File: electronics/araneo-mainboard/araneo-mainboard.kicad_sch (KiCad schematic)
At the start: 69 parts, among them J2 OLED, J3 GPIO, SW1 SW, SW2 SW, U1 IMU, U2 L78M05CDT, U3 BD9C601EFJ, U4 POWER, U5 PAM8403D

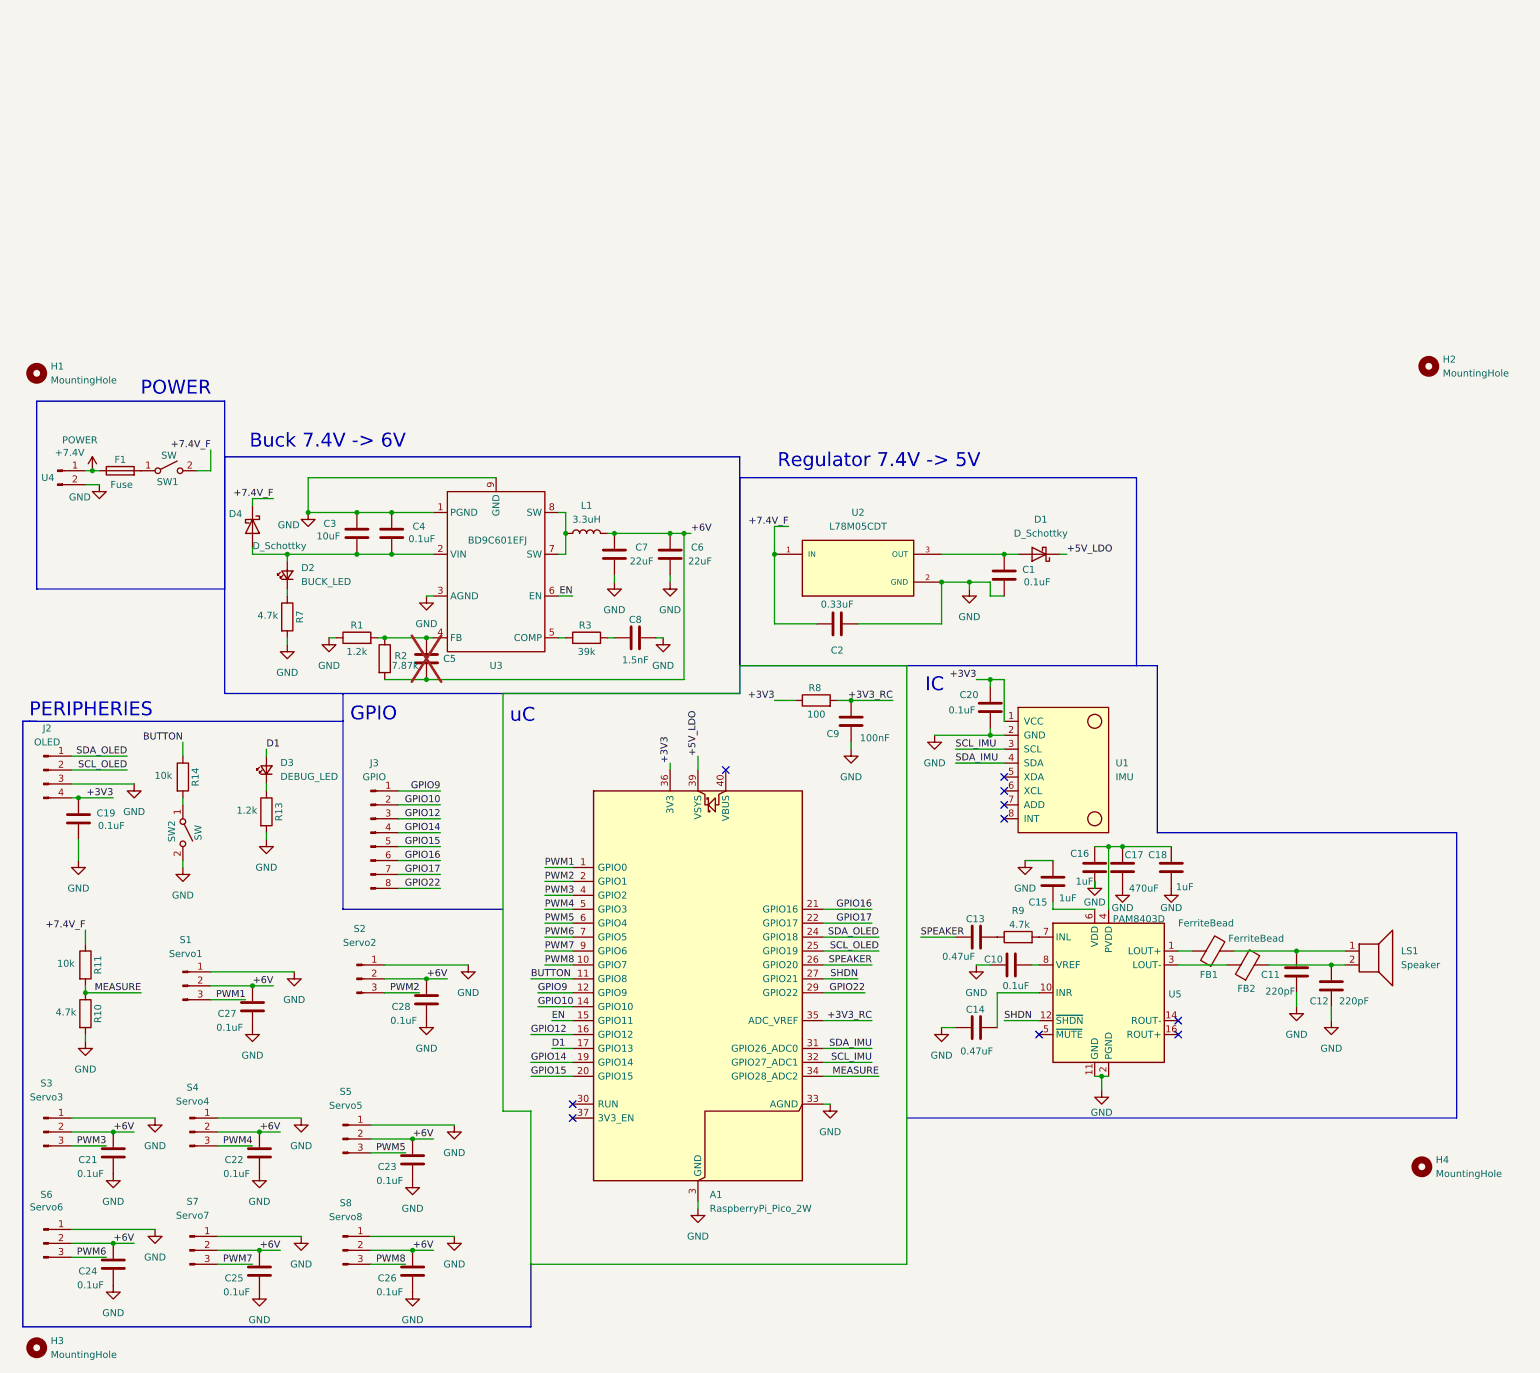
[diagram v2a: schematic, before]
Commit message: electronics: new buck, regulator and improve schematic
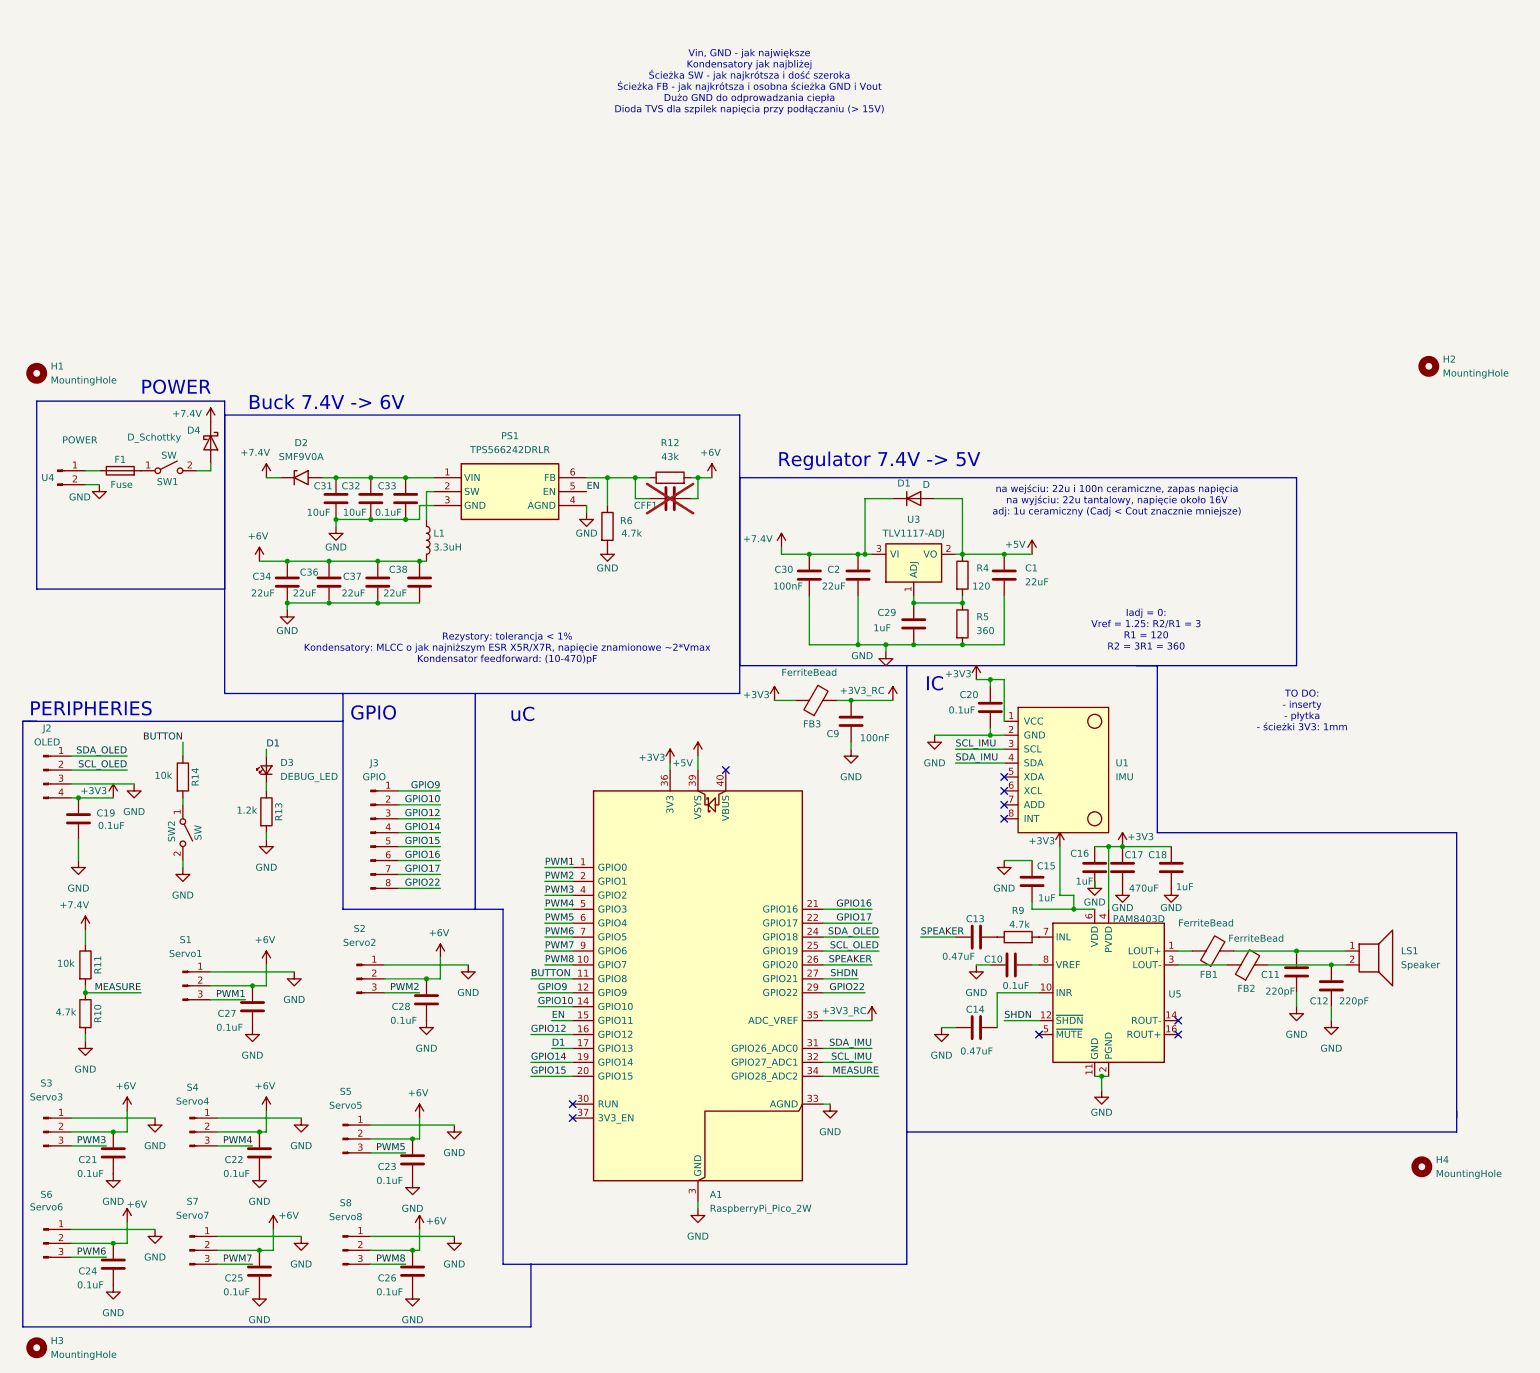
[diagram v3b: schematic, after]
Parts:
- removed C3: 10uF, Capacitor_SMD:C_1206_3216Metric_Pad1.33x1.80mm_HandSolder, symbol Device:C
- removed C4: 0.1uF, Capacitor_SMD:C_0603_1608Metric_Pad1.08x0.95mm_HandSolder, symbol Device:C
- removed C5: OPEN, Capacitor_SMD:C_0603_1608Metric_Pad1.08x0.95mm_HandSolder, symbol Device:C
- removed C6, C7: 22uF, Capacitor_SMD:C_1210_3225Metric_Pad1.33x2.70mm_HandSolder, symbol Device:C
- removed C8: 1.5nF, Capacitor_SMD:C_0603_1608Metric_Pad1.08x0.95mm_HandSolder, symbol Device:C
- removed D1: D_Schottky, Diode_THT:D_DO-41_SOD81_P10.16mm_Horizontal, symbol Device:D_Schottky
- removed D2: BUCK_LED, PCM_SparkFun-LED:LED_0603_1608Metric, symbol PCM_SparkFun-LED:LED
- removed R1: 1.2k, Resistor_SMD:R_0603_1608Metric_Pad0.98x0.95mm_HandSolder, symbol Device:R
- removed R2: 7.87k, Resistor_SMD:R_0603_1608Metric_Pad0.98x0.95mm_HandSolder, symbol Device:R
- removed R3: 39k, Resistor_SMD:R_0603_1608Metric_Pad0.98x0.95mm_HandSolder, symbol Device:R
- removed R7: 4.7k, Resistor_SMD:R_0603_1608Metric_Pad0.98x0.95mm_HandSolder, symbol Device:R
- removed R8: 100, Resistor_SMD:R_0603_1608Metric_Pad0.98x0.95mm_HandSolder, symbol Device:R
- removed U2: L78M05CDT, custom_footprints:VREG_L78M05CDT, symbol Symbols:L78M05CDT
- removed U3: BD9C601EFJ, custom_footprints:SOIC127P600X100-9N, symbol Custom_Regulators:BD9C601EFJ
- added C29: 1uF, Capacitor_SMD:C_0603_1608Metric_Pad1.08x0.95mm_HandSolder, symbol Device:C
- added C30, CFF1: 100nF, Capacitor_SMD:C_0603_1608Metric_Pad1.08x0.95mm_HandSolder, symbol Device:C
- added C31, C32: 10uF, Capacitor_SMD:C_1206_3216Metric_Pad1.33x1.80mm_HandSolder, symbol Device:C
- added C33: 0.1uF, Capacitor_SMD:C_0201_0603Metric_Pad0.64x0.40mm_HandSolder, symbol Device:C
- added C34, C36, C37, C38: 22uF, Capacitor_SMD:C_1210_3225Metric_Pad1.33x2.70mm_HandSolder, symbol Device:C
- added D1: D, Diode_THT:D_DO-41_SOD81_P10.16mm_Horizontal, symbol Device:D
- added D2: SMF9V0A, Diode_SMD:D_SMF, symbol Diode:SMF9V0A
- added FB3: FerriteBead, Resistor_SMD:R_0603_1608Metric_Pad0.98x0.95mm_HandSolder, symbol Device:FerriteBead
- added PS1: TPS566242DRLR, custom_footprints:SOT50P160X60-6N, symbol Symbols:TPS566242DRLR
- added R12: 43k, Resistor_SMD:R_0603_1608Metric_Pad0.98x0.95mm_HandSolder, symbol Device:R
- added R4: 120, Resistor_SMD:R_0603_1608Metric_Pad0.98x0.95mm_HandSolder, symbol Device:R
- added R5: 360, Resistor_SMD:R_0603_1608Metric_Pad0.98x0.95mm_HandSolder, symbol Device:R
- added R6: 4.7k, Resistor_SMD:R_0603_1608Metric_Pad0.98x0.95mm_HandSolder, symbol Device:R
- added U3: TLV1117-ADJ, Package_TO_SOT_SMD:SOT-223-3_TabPin2, symbol Regulator_Linear:TLV1117-ADJ
- C1: value 0.1uF -> 22uF; footprint Capacitor_SMD:C_0603_1608Metric_Pad1.08x0.95mm_HandSolder -> Capacitor_Tantalum_SMD:CP_EIA-3528-15_AVX-H_HandSolder
- C2: value 0.33uF -> 22uF; footprint Capacitor_SMD:C_0805_2012Metric_Pad1.18x1.45mm_HandSolder -> Capacitor_SMD:C_1210_3225Metric_Pad1.33x2.70mm_HandSolder
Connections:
- net +5V_LDO is gone; now on net +5V: A1.39 (VSYS)
- net +3V3: now also C15.1, C16.2, C17.2, C18.2, U5.13 (PVDD), U5.4 (PVDD), U5.6 (VDD), FB3.1
- net +3V3_RC: now also FB3.2
- net +6V: now also C34.1, C36.1, C37.1, C38.1, CFF1.2, R12.2
- net +7.4V: now also C2.1, D4.1 (K), R11.1, C30.1, D1.1 (K), D2.1 (A1), U3.3 (VI); no longer F1.1, U4.1 (Pin_1)
- net EN: now also PS1.5 (EN)
- net GND: now also C29.2, C30.2, C31.2, C32.2, C33.2, C34.2, C36.2, C37.2, C38.2, PS1.3 (GND), PS1.4 (AGND), R5.2, R6.2
- net at D4.2 (A): now also SW1.2 (B)
- net at L1.1: now also PS1.2 (SW)
- net +5V: now reaches C1.1
- net +5V: now also D1.2 (A), R4.1, U3.2 (VO)
- removed net +7.4V_F: C2.1, D4.1 (K), R11.1, SW1.2 (B)
- new net: F1.1, U4.1 (Pin_1)
- new net: CFF1.1, PS1.6 (FB), R12.1, R6.1
- new net: C31.1, C32.1, C33.1, D2.2 (A2), PS1.1 (VIN)
- new net: C29.1, R4.2, R5.1, U3.1 (ADJ)
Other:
- note added: "Iadj = 0: Vref = 1.25: R2/R1 = 3 R1 = 120 R2 = 3R1 = 360"
- note added: "Rezystory: tolerancja < 1% Kondensatory: MLCC o jak najniższym ESR X5R/X7R, napięcie znamionowe ~2*Vmax Kondensator feedforward: (10-470)pF"
- note added: "TO DO: - inserty - płytka - ścieżki 3V3: 1mm"
- note added: "Vin, GND - jak największe Kondensatory jak najbliżej Ścieżka SW - jak najkrótsza i dość szeroka Ścieżka FB - jak najkrótsza i osobna ścieżka GND i Vout Dużo GND do odprowadzania ciepła Dioda TVS dla szpilek napięcia przy podłączaniu (> 15V)"
- note added: "na wejściu: 22u i 100n ceramiczne, zapas napięcia na wyjściu: 22u tantalowy, napięcie około 16V adj: 1u ceramiczny (Cadj < Cout znacznie mniejsze)"
- moved on the sheet: C15

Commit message: electronics: pcb v3
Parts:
- removed D4: D_Schottky, Diode_THT:D_DO-41_SOD81_P10.16mm_Horizontal, symbol Device:D_Schottky
- removed F1: Fuse, custom_footprints:3568, symbol Device:Fuse
- removed J3: GPIO, Connector_PinHeader_2.54mm:PinHeader_1x08_P2.54mm_Vertical, symbol Connector:Conn_01x08_Pin
- removed SW1: SW, PCM_SparkFun-Connector:ScrewTerminal_1x02_P5.0mm, symbol Switch:SW_SPST
- added D5: POWER_LED, PCM_SparkFun-LED:LED_0603_1608Metric, symbol PCM_SparkFun-LED:LED
- added D6: D_Schottky, Diode_THT:D_DO-41_SOD81_P10.16mm_Horizontal, symbol Device:D_Schottky
- added F2: Fuse, custom_footprints:3568, symbol Device:Fuse
- added J1: GPIO2, Connector_PinHeader_2.54mm:PinHeader_1x06_P2.54mm_Vertical, symbol Connector:Conn_01x06_Pin
- added J3: GPIO1, Connector_PinHeader_2.54mm:PinHeader_1x02_P2.54mm_Vertical, symbol Connector:Conn_01x02_Pin
- added R15: 1k, Resistor_SMD:R_0603_1608Metric_Pad0.98x0.95mm_HandSolder, symbol Device:R
- added SW3: SW, PCM_SparkFun-Connector:ScrewTerminal_1x02_P5.0mm, symbol Switch:SW_SPST
- C33: footprint Capacitor_SMD:C_0201_0603Metric_Pad0.64x0.40mm_HandSolder -> Capacitor_SMD:C_0603_1608Metric_Pad1.08x0.95mm_HandSolder
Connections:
- net GPIO16 is gone; now on net SDA_OLED: A1.21 (GPIO16)
- net GPIO17 is gone; now on net SCL_OLED: A1.22 (GPIO17)
- net GPIO22 is gone; now on net D1: A1.29 (GPIO22)
- net GPIO9 is gone; now on net PWM8: A1.12 (GPIO9)
- net +7.4V: now also U4.1 (Pin_1), D6.1 (K); no longer C2.1, C30.1, D1.1 (K), D2.1 (A1), R11.1, U3.3 (VI)
- net BUTTON: now also A1.2 (GPIO1); no longer A1.11 (GPIO8)
- net D1: no longer A1.17 (GPIO13)
- net EN: now also A1.1 (GPIO0); no longer A1.15 (GPIO11)
- net GND: now also R15.1
- net GPIO10: now also J1.1 (Pin_1)
- net GPIO12: now also J1.3 (Pin_3)
- net GPIO14: now also J1.5 (Pin_5)
- net GPIO15: now also J1.6 (Pin_6)
- net PWM1: now also A1.4 (GPIO2); no longer A1.1 (GPIO0)
- net PWM2: now also A1.5 (GPIO3); no longer A1.2 (GPIO1)
- net PWM3: now also A1.6 (GPIO4); no longer A1.4 (GPIO2)
- net PWM4: now also A1.7 (GPIO5); no longer A1.5 (GPIO3)
- net PWM5: now also A1.9 (GPIO6); no longer A1.6 (GPIO4)
- net PWM6: now also A1.10 (GPIO7); no longer A1.7 (GPIO5)
- net PWM7: now also A1.11 (GPIO8); no longer A1.9 (GPIO6)
- net PWM8: no longer A1.10 (GPIO7)
- net SCL_OLED: no longer A1.25 (GPIO19)
- net SDA_OLED: no longer A1.24 (GPIO18)
- net SHDN: now also A1.26 (GPIO20); no longer A1.27 (GPIO21)
- net SPEAKER: now also A1.27 (GPIO21); no longer A1.26 (GPIO20)
- net at C31.1, C32.1, C33.1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: now also D5.2 (A)
- new net: F2.2, SW3.2 (B)
- new net: D6.2 (A), SW3.1 (A)
- new net: D5.1 (K), R15.2
- new net +7.4V_F: C2.1, C30.1, D1.1 (K), D2.1 (A1), F2.1, R11.1, U3.3 (VI)
- new net GPIO11: A1.15 (GPIO11), J1.2 (Pin_2)
- new net GPIO13: A1.17 (GPIO13), J1.4 (Pin_4)
- new net GPIO18: A1.24 (GPIO18), J3.1 (Pin_1)
- new net GPIO19: A1.25 (GPIO19), J3.2 (Pin_2)
